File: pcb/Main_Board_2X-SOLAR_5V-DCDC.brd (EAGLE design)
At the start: 86.4 x 35.7 mm, 105 parts, among them CN1 DCIN, CN5 USBA_FEMALE, CN6 MicroUSB, IC1 MCP73871, IC2 MCP73871, T2 MMUN2133LT1G, U3 TPS61090RSAR, U4 MCP73871

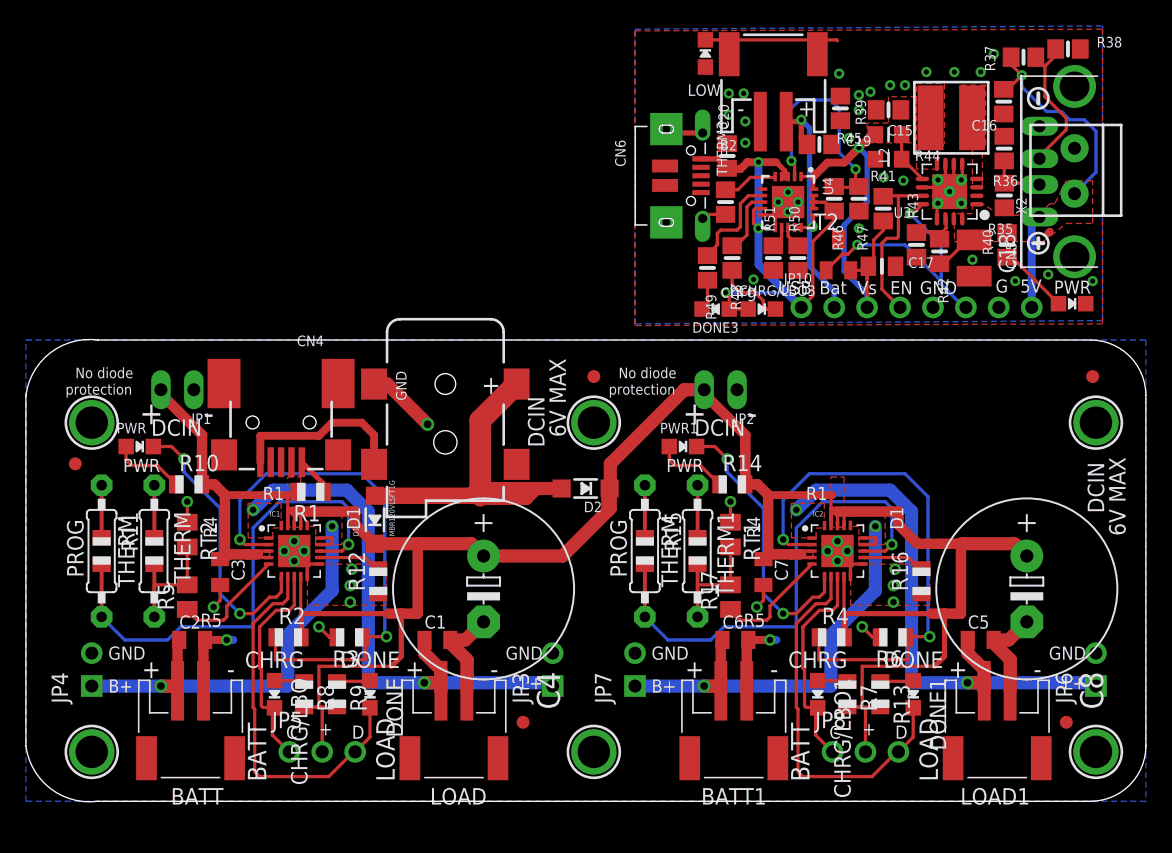
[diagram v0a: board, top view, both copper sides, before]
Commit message: Added 5V board and fixed PCB layout
Added 5V step up board loayout to main PCB. Removed additional MCP module from 5V layout.
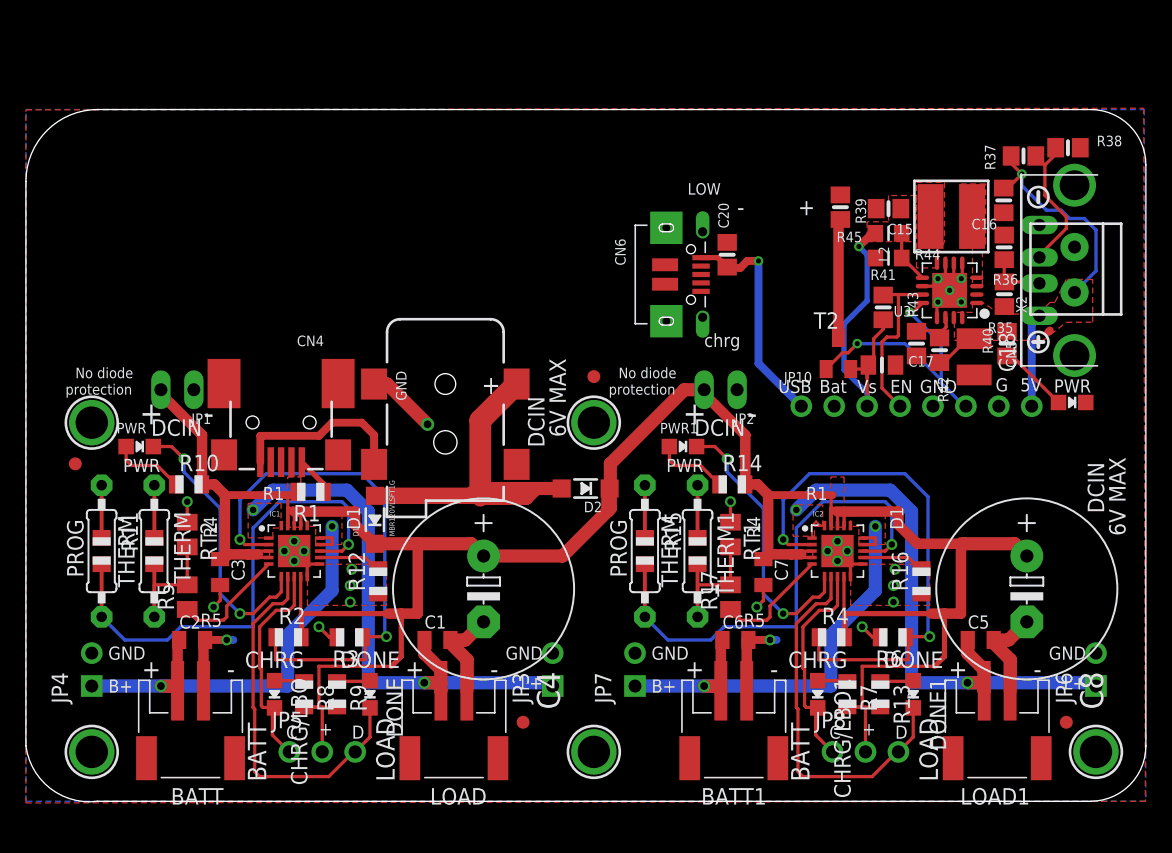
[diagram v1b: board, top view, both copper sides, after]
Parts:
- removed B2: JST 2-PH, microbuilder:JSTPH2
- removed C19: 10uF, microbuilder:0805-NO
- removed CHRG/LBO3: ORANGE, microbuilder:CHIPLED_0805_NOOUTLINE
- removed DONE3: GREEN, microbuilder:CHIPLED_0805_NOOUTLINE
- removed LED3: RED, microbuilder:CHIPLED_0805_NOOUTLINE
- removed R46: 270K, microbuilder:0805-NO
- removed R47, R51: 100K, microbuilder:0805-NO
- removed R48, R49: 1K, microbuilder:0805-NO
- removed R50: 1.0K, microbuilder:0805-NO
- removed THERM3: 15K, microbuilder:0805-NO
- removed U$1, U$16: (no value), microbuilder:ADAFRUIT_TEXT_20MM
- removed U$14: MOUNTINGHOLE2.5, microbuilder:MOUNTINGHOLE_2.5_PLATED
- removed U$15: FIDUCIAL, adafruit:FIDUCIAL_1MM
- removed U4: MCP73871, microbuilder:QFN20_4MM
- moved C15 7.62 mm to (66.5, 45.7)
- moved C16 7.62 mm to (75.4, 46.4)
- moved L2 7.62 mm to (71.4, 45.1)
- moved LED4 7.62 mm to (80.7, 30.8)
- moved R35 7.62 mm to (75.5, 39.1)
- moved R36 7.62 mm to (75.5, 42.7)
- moved R37 7.62 mm to (77.0, 49.8)
- moved R38 7.62 mm to (80.4, 50.4)
- moved R39 7.62 mm to (62.8, 45.8)
- moved R40 7.62 mm to (75.7, 35.3)
- moved R41 7.62 mm to (66.1, 38.1)
- moved R43 7.62 mm to (68.7, 35.3)
- moved R44 7.62 mm to (66.5, 41.9)
- moved R45 7.62 mm to (66.5, 43.8)
- moved T2 7.62 mm to (62.7, 34.5)
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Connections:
- net N$3 renamed GNDBREAK
- removed net N$45: R46.1, R47.1, U4.P$2
- removed net N$46: R49.1, U4.P$7
- removed net N$47: R48.1, U4.P$8
- removed net N$48: R50.2, U4.P$13
- removed net N$49: THERM3.2, U4.P$5
- removed net N$50: DONE3.C, R49.2
- removed net N$51: CHRG/LBO3.C, R48.2
- removed net N$52: R51.2, U4.P$12
- removed net VLIPO: B2.2, C19.1, JP10.2, U4.P$14, U4.P$15, U4.P$16
- new net N$26: R39.2, T2.C
- net GND: now also C17.2, R39.1; no longer B2.1, C19.2, R50.1, THERM3.1, U4.P$10, U4.P$11, U4.P$21
- net VBAT: now also R41.1; no longer U4.P$1, U4.P$20
- net VBUS: no longer CHRG/LBO3.A, DONE3.A, U4.P$17, U4.P$18, U4.P$19, U4.P$3, U4.P$4, U4.P$9
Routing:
- net VBUS: track 42.5 -> 17.6 mm, vias 3 -> 1
- net VLIPO: track 21.5 -> 0.00 mm, vias 2 -> 0
- net N$45: track 18.4 -> 0.00 mm, vias 2 -> 0
- net GND: track 78.6 -> 60.5 mm, vias 51 -> 23
- net N$26: track 0.00 -> 9.28 mm
- net N$46: track 7.78 -> 0.00 mm
- net VBAT: track 30.9 -> 24.5 mm
- net N$51: track 5.43 -> 0.00 mm
- net N$47: track 5.01 -> 0.00 mm
- net N$49: track 4.29 -> 0.00 mm
- net N$50: track 2.40 -> 0.00 mm
- net OUT1: track 43.5 -> 45.7 mm
- net N$48: track 1.72 -> 0.00 mm
- net N$52: track 1.67 -> 0.00 mm
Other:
- board size 86.4 x 35.7 mm -> 86.4 x 53.4 mm

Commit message: Completed board layout
Completed layout for 2 MCP chips and TI 5V step-up boost. MCP load outputs merged and routed to 5V step-up, no 5V power wires needed. Added terminal block option for solar panel input. Added BOM folder and PCB quotes spreadsheet.
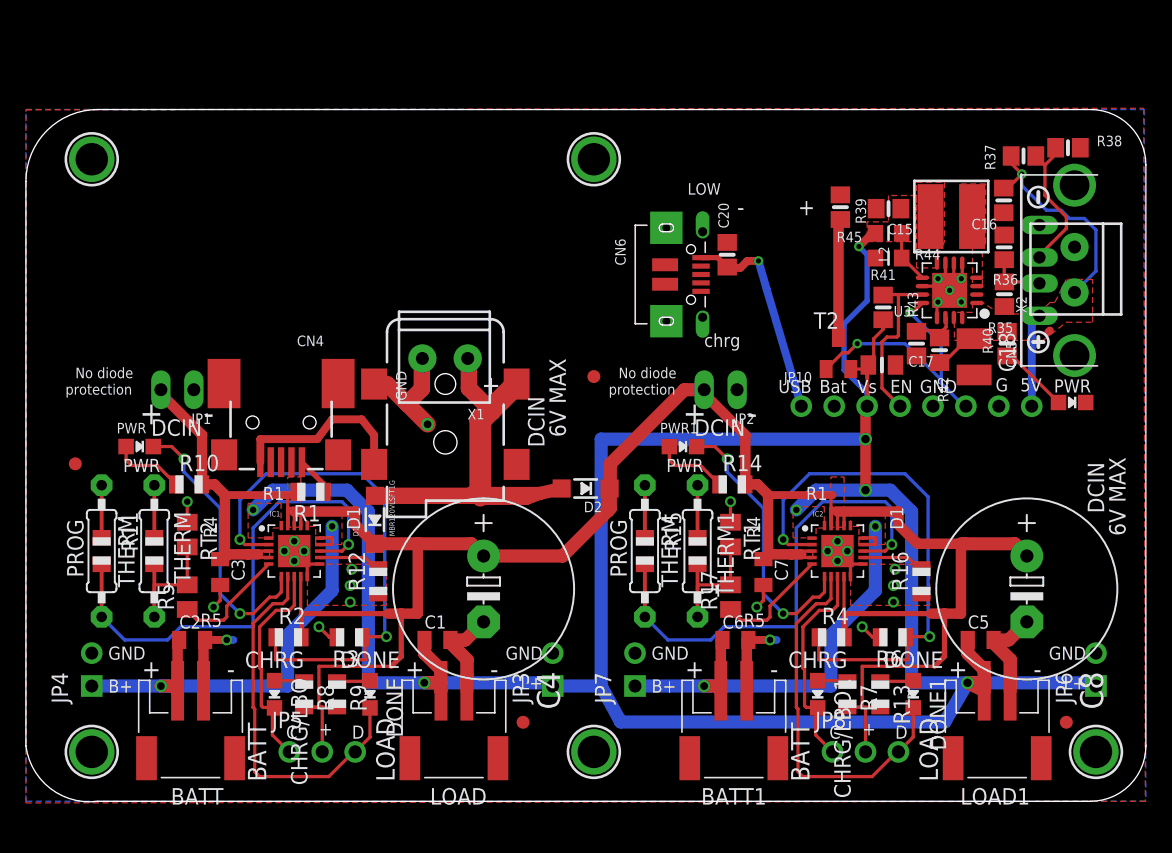
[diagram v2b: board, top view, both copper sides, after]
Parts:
- added X1: (no value), microbuilder:TERMBLOCK_1X2-3.5MM
- moved U$6 20.3 mm to (5.08, 49.5)
- moved U$7 20.3 mm to (43.8, 49.5)
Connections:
- net N$39 renamed SW
- net N$40 renamed LBI
- net N$6 renamed VPCC
- net N$7 renamed VPCC1
- removed net OUT: C1.1, IC1.P$1, IC1.P$20, JP3.1, LOAD.1
- removed net OUT1: C5.1, IC2.P$1, IC2.P$20, JP6.1, LOAD1.1
- net GND: now also X1.1
- net PV_IN: now also X1.2
- net VBAT: now also C1.1, C5.1, IC1.P$1, IC1.P$20, IC2.P$1, IC2.P$20, JP3.1, JP6.1, LOAD.1, LOAD1.1
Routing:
- net VBAT: track 24.5 -> 194.5 mm, vias 1 -> 7
- net OUT1: track 45.7 -> 0.00 mm, vias 2 -> 0
- net OUT: track 43.5 -> 0.00 mm, vias 2 -> 0
- net GND: track 60.5 -> 68.9 mm
- net PV_IN: track 29.4 -> 34.4 mm
- net VBUS: track 17.6 -> 16.7 mm
- removed copper zone on layer 1, net OUT
- removed copper zone on layer 1, net OUT1

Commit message: PCB board rev 1
Files used to print prototype from bayareacircuits. Adding BOM file and CAM/GERBER files
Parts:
- R11, R15: value 2K -> 1K
- moved U$6 1.27 mm to (5.08, 48.3)
- moved U$7 1.27 mm to (43.8, 48.3)
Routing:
- net VBAT: track 194.5 -> 162.8 mm
- added copper zone on layer 1, net N$3
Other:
- board size 86.4 x 53.4 mm -> 86.4 x 52.1 mm
- board text removed: "LOW"
- board text removed: "No diode"
- board text removed: "chrg"
- board text removed: "protection"
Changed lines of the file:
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@@
 </layers>
 <board>
+<description>Rainforest Connection Power Board Rev 1</description>
 <plain>
 <wire x1="20.3962" y1="21.4122" x2="20.5232" y2="21.4122" width="0.0254" layer="41"/>
@@
 <wire x1="34.163" y1="8.001" x2="10.033" y2="8.001" width="0.4064" layer="22"/>
 <wire x1="0" y1="4.27" x2="0" y2="47.827" width="0" layer="20"/>
-<wire x1="0" y1="47.827" x2="5.54" y2="53.367" width="0" layer="20" curve="-90"/>
-<wire x1="5.54" y1="53.367" x2="82.132" y2="53.367" width="0" layer="20"/>
-<wire x1="82.132" y1="53.367" x2="86.402" y2="49.097" width="0" layer="20" curve="-90"/>
-<wire x1="86.402" y1="49.097" x2="86.402" y2="4.27" width="0" layer="20"/>
+<wire x1="0" y1="47.827" x2="4.27" y2="52.097" width="0" layer="20" curve="-90"/>
+<wire x1="4.27" y1="52.097" x2="80.862" y2="52.097" width="0" layer="20"/>
+<wire x1="80.862" y1="52.097" x2="86.402" y2="46.557" width="0" layer="20" curve="-90"/>
+<wire x1="86.402" y1="46.557" x2="86.402" y2="4.27" width="0" layer="20"/>
 <wire x1="86.402" y1="4.27" x2="82.132" y2="0" width="0" layer="20" curve="-90"/>
 <wire x1="82.132" y1="0" x2="5.54" y2="0" width="0" layer="20"/>
@@
 <text x="25.146" y="4.826" size="1.016" layer="21" font="vector" ratio="10">D</text>
 <text x="22.606" y="5.08" size="1.016" layer="21" font="vector" ratio="10">+</text>
-<text x="3.81" y="32.639" size="0.8128" layer="21" font="vector">No diode</text>
-<text x="3.048" y="31.369" size="0.8128" layer="21" font="vector">protection</text>
 <wire x1="62.3062" y1="21.4122" x2="62.4332" y2="21.4122" width="0.0254" layer="41"/>
 <wire x1="62.4332" y1="21.4122" x2="62.4332" y2="21.082" width="0.0254" layer="41"/>
@@
 <text x="67.056" y="4.826" size="1.016" layer="21" font="vector" ratio="10">D</text>
 <text x="64.516" y="5.08" size="1.016" layer="21" font="vector" ratio="10">+</text>
-<text x="45.72" y="32.639" size="0.8128" layer="21" font="vector">No diode</text>
-<text x="44.958" y="31.369" size="0.8128" layer="21" font="vector">protection</text>
-<text x="52.324" y="47.244" size="0.889" layer="21" ratio="12" rot="R180" align="center">LOW</text>
 <text x="80.74" y="32.041" size="1.016" layer="21" ratio="12" rot="R180" align="center">PWR</text>
 <text x="68.961" y="31.496" size="1.016" layer="21" ratio="12">GND</text>
@@
 <text x="74.549" y="31.496" size="1.016" layer="22" ratio="12" rot="MR90">GND</text>
 <text x="76.962" y="31.623" size="1.016" layer="22" ratio="12" rot="MR90">5Vo</text>
-<text x="52.324" y="35.052" size="1.016" layer="21" ratio="12">chrg</text>
 <text x="61.214" y="31.496" size="1.016" layer="21" ratio="12">Bat</text>
 <text x="58.039" y="31.496" size="1.016" layer="21" ratio="12">USB</text>
 <text x="64.135" y="31.496" size="1.016" layer="21" ratio="12">Vs</text>
-<text x="59.563" y="45.212" size="1.27" layer="21" ratio="12">+</text>
-<text x="54.864" y="45.212" size="1.27" layer="21" ratio="12">-</text>
 <text x="59.182" y="31.496" size="1.016" layer="22" ratio="12" rot="MR90">USB</text>
 <text x="64.516" y="31.496" size="1.016" layer="22" ratio="12" rot="MR90">Vsh</text>
@@
 <attribute name="VALUE" x="15.24" y="12.446" size="1.27" layer="27" font="vector" rot="R180"/>
 </element>
-<element name="R11" library="adafruit" package="0805-THM" value="2K" x="5.842" y="19.304" smashed="yes" rot="R270">
+<element name="R11" library="adafruit" package="0805-THM" value="1K" x="5.842" y="19.304" smashed="yes" rot="R270">
 <attribute name="NAME" x="7.366" y="22.352" size="1.27" layer="25" ratio="10" rot="R270"/>
 <attribute name="VALUE" x="4.553" y="18.0784" size="1.27" layer="27" font="vector" ratio="10" rot="R90"/>
@@
 <element name="U$4" library="microbuilder" package="MOUNTINGHOLE_2.5_PLATED" value="MOUNTINGHOLE2.5" x="5.08" y="3.81"/>
 <element name="U$5" library="microbuilder" package="MOUNTINGHOLE_2.5_PLATED" value="MOUNTINGHOLE2.5" x="43.815" y="3.81"/>
-<element name="U$6" library="microbuilder" package="MOUNTINGHOLE_2.5_PLATED" value="MOUNTINGHOLE2.5" x="5.08" y="49.53"/>
-<element name="U$7" library="microbuilder" package="MOUNTINGHOLE_2.5_PLATED" value="MOUNTINGHOLE2.5" x="43.815" y="49.53"/>
+<element name="U$6" library="microbuilder" package="MOUNTINGHOLE_2.5_PLATED" value="MOUNTINGHOLE2.5" x="5.08" y="48.26"/>
+<element name="U$7" library="microbuilder" package="MOUNTINGHOLE_2.5_PLATED" value="MOUNTINGHOLE2.5" x="43.815" y="48.26"/>
 <element name="JP5" library="adafruit" package="1X03-CLEANBIG" value="" x="22.86" y="3.81"/>
 <element name="U$8" library="adafruit" package="FIDUCIAL_1MM" value="FIDUCIAL" x="43.815" y="32.766"/>
@@
 <attribute name="VALUE" x="57.15" y="12.446" size="1.27" layer="27" font="vector" rot="R180"/>
 </element>
-<element name="R15" library="adafruit" package="0805-THM" value="2K" x="47.752" y="19.304" smashed="yes" rot="R270">
+<element name="R15" library="adafruit" package="0805-THM" value="1K" x="47.752" y="19.304" smashed="yes" rot="R270">
 <attribute name="NAME" x="49.276" y="22.352" size="1.27" layer="25" ratio="10" rot="R270"/>
 <attribute name="VALUE" x="46.463" y="18.0784" size="1.27" layer="27" font="vector" ratio="10" rot="R90"/>
@@
 <element name="R37" library="microbuilder" package="0805-NO" value="75K 1%" x="76.962" y="49.784" smashed="yes" rot="R180">
 <attribute name="NAME" x="74.792" y="48.6965" size="0.8128" layer="25" ratio="18" rot="R90"/>
-<attribute name="VALUE" x="78.2324" y="53.645" size="1.016" layer="27" font="vector" ratio="10" rot="R180"/>
+<attribute name="VALUE" x="76.4544" y="54.026" size="1.016" layer="27" font="vector" ratio="10" rot="R180"/>
 </element>
 <element name="R38" library="microbuilder" package="0805-NO" value="49.9K 1%" x="80.391" y="50.419" smashed="yes">
-<attribute name="NAME" x="84.5785" y="51.349" size="0.8128" layer="25" ratio="18" rot="R180"/>
-<attribute name="VALUE" x="79.2576" y="52.651" size="1.016" layer="27" font="vector" ratio="10"/>
+<attribute name="NAME" x="84.5785" y="50.079" size="0.8128" layer="25" ratio="18" rot="R180"/>
+<attribute name="VALUE" x="80.1466" y="53.032" size="1.016" layer="27" font="vector" ratio="10"/>
 </element>
 <element name="CN5" library="microbuilder" package="USB_HOST-PTH" value="USBA_FEMALE" x="84.709" y="40.9575" smashed="yes" rot="R90">
@@
 <polygon width="0.254" layer="16" isolate="0.254">
 <vertex x="0" y="0"/>
-<vertex x="0" y="53.367"/>
-<vertex x="86.275" y="53.367"/>
+<vertex x="0" y="52.097"/>
+<vertex x="86.275" y="52.097"/>
 <vertex x="86.402" y="0"/>
 </polygon>
@@
 <polygon width="0.254" layer="1" spacing="0.254" isolate="0.254" rank="2">
 <vertex x="0" y="-0.127"/>
-<vertex x="0" y="53.34"/>
-<vertex x="86.233" y="53.467"/>
+<vertex x="0" y="52.07"/>
+<vertex x="86.233" y="52.197"/>
 <vertex x="86.36" y="0"/>
 </polygon>
@@
 <wire x1="64.77" y1="27.94" x2="64.77" y2="24.003" width="0.8128" layer="1"/>
 <wire x1="40.64" y1="8.89" x2="44.37965625" y2="8.89" width="1.016" layer="16"/>
-<wire x1="44.37965625" y1="8.89" x2="45.87825625" y2="6.1214" width="1.016" layer="16"/>
-<wire x1="45.87825625" y1="6.1214" x2="70.8914" y2="6.1214" width="1.016" layer="16"/>
-<wire x1="70.8914" y1="6.1214" x2="72.644" y2="9.144" width="1.016" layer="16"/>
 <via x="72.644" y="9.144" extent="1-16" drill="0.65"/>
 <polygon width="0.254" layer="1">
@@
 <wire x1="62.6872" y1="44.883" x2="62.833" y2="44.883" width="0.8128" layer="1"/>
 </signal>
+<signal name="N$3">
+<polygon width="0.3048" layer="1" spacing="0.4064">
+<vertex x="19.05" y="20.32"/>
+<vertex x="17.78" y="20.32"/>
+<vertex x="17.78" y="21.59"/>
+<vertex x="19.05" y="21.59"/>
+</polygon>
+</signal>
 </signals>
